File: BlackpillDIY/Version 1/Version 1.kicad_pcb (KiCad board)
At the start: 2 copper layers, 1 part, among them U1 STM32F411CCUx

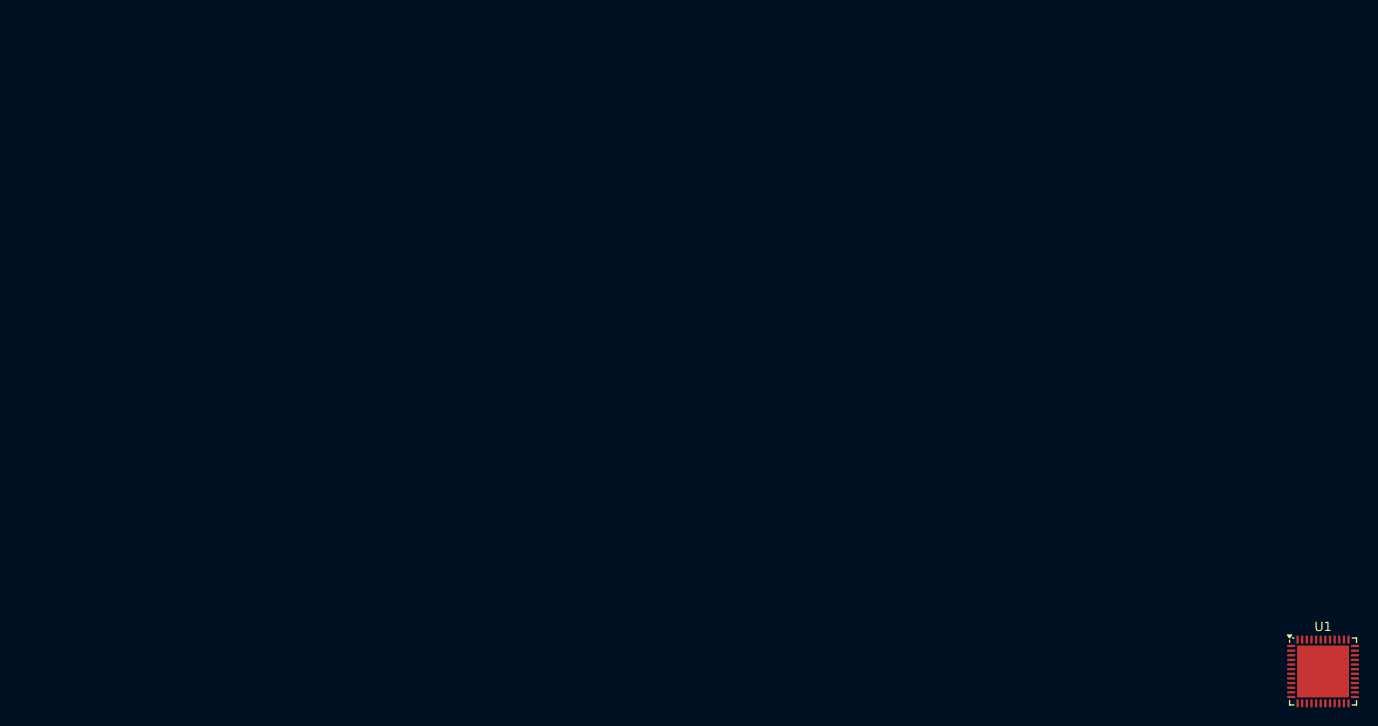
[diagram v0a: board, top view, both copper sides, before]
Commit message: Created THT PCB
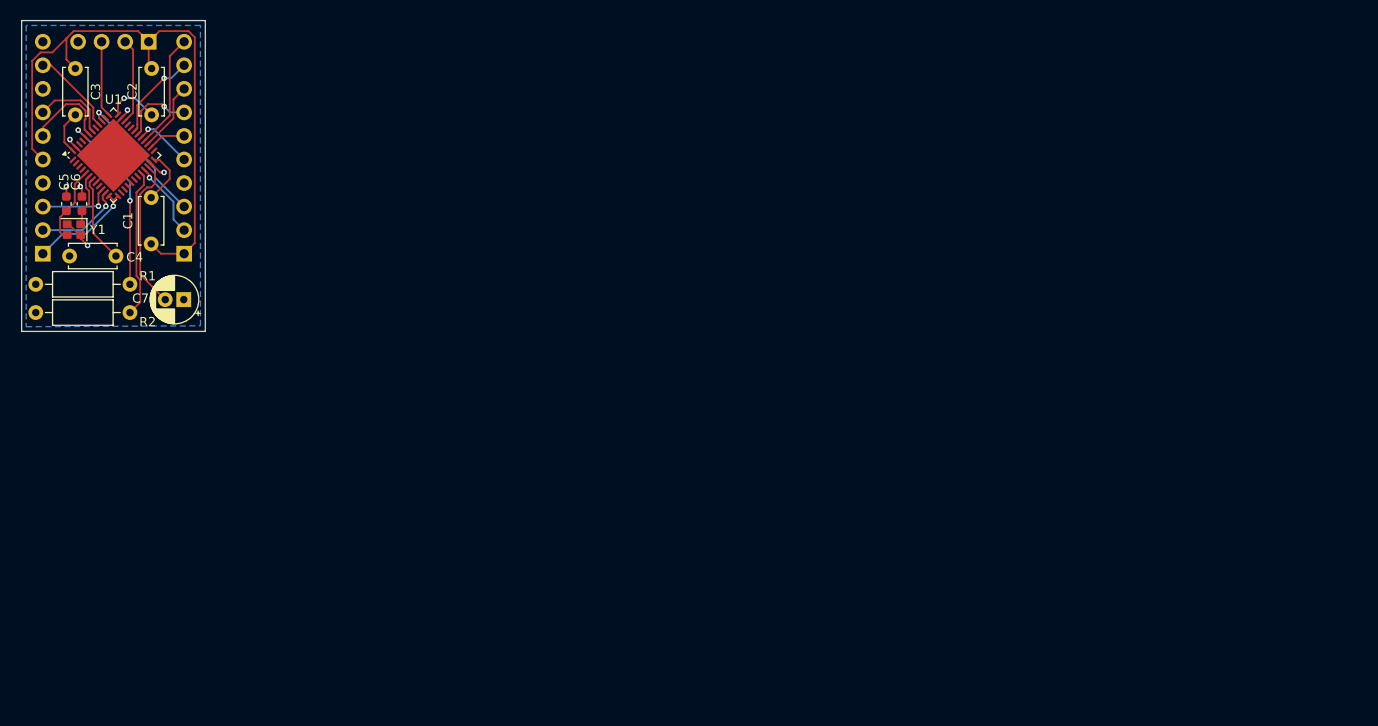
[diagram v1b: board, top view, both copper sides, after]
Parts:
- added C1: 100n, Capacitor_THT:C_Disc_D5.0mm_W2.5mm_P5.00mm, F.Cu at (27.6, 37.5)
- added C2: 100n, Capacitor_THT:C_Disc_D5.0mm_W2.5mm_P5.00mm, F.Cu at (27.7, 18.6)
- added C3: 100n, Capacitor_THT:C_Disc_D5.0mm_W2.5mm_P5.00mm, F.Cu at (19.5, 18.6)
- added C4: 100n, Capacitor_THT:C_Disc_D5.0mm_W2.5mm_P5.00mm, F.Cu at (18.8, 38.8)
- added C5: 12p, Capacitor_SMD:C_0603_1608Metric, F.Cu at (18.5, 33.2)
- added C6: 12p, Capacitor_SMD:C_0603_1608Metric, F.Cu at (20.2, 33.2)
- added C7: 2.2u, Capacitor_THT:CP_Radial_D5.0mm_P2.00mm, F.Cu at (31.2, 43.5)
- added J1: Left Header, Connector_PinHeader_2.54mm:PinHeader_1x10_P2.54mm_Vertical, B.Cu at (16.0, 38.5)
- added J2: Right Header, Connector_PinHeader_2.54mm:PinHeader_1x10_P2.54mm_Vertical, B.Cu at (31.2, 38.5)
- added J3: Debug, Connector_PinHeader_2.54mm:PinHeader_1x04_P2.54mm_Vertical, B.Cu at (27.4, 15.7)
- added R1: 10k, Resistor_THT:R_Axial_DIN0207_L6.3mm_D2.5mm_P10.16mm_Horizontal, F.Cu at (15.2, 41.8)
- added R2: 10k, Resistor_THT:R_Axial_DIN0207_L6.3mm_D2.5mm_P10.16mm_Horizontal, F.Cu at (15.2, 44.9)
- added Y1: Crystal_GND24, Crystal:Crystal_SMD_SeikoEpson_FA128-4Pin_2.0x1.6mm, F.Cu at (19.3, 36.0)
- moved U1 141.9 mm to (23.6, 27.9), turned to 45 degrees
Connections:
- U1 pad 10: unconnected-(U1-PA0-Pad10) -> TIM2_CH1
- U1 pad 11: unconnected-(U1-PA1-Pad11) -> TIM2_CH2
- U1 pad 12: unconnected-(U1-PA2-Pad12) -> TIM2_CH3
- U1 pad 13: unconnected-(U1-PA3-Pad13) -> TIM2_CH3
- U1 pad 20: unconnected-(U1-PB2-Pad20) -> /BOOT1
- U1 pad 21: unconnected-(U1-PB10-Pad21) -> I2C2_SCL
- U1 pad 22: unconnected-(U1-VCAP1-Pad22) -> /VCAP
- U1 pad 23: Net-(U1-VSS-Pad23) -> GND
- U1 pad 24: unconnected-(U1-VDD-Pad24) -> /VDD1
- U1 pad 26: unconnected-(U1-PB13-Pad26) -> TIM1_CH1N
- U1 pad 27: Net-(U1-PB14) -> TIM1_CH2N
- U1 pad 28: Net-(U1-PB15) -> TIM1_CH3N
- U1 pad 29: unconnected-(U1-PA8-Pad29) -> TIM1_CH1
- U1 pad 30: unconnected-(U1-PA9-Pad30) -> TIM1_CH2
- U1 pad 31: unconnected-(U1-PA10-Pad31) -> TIM1_CH3
- U1 pad 34: unconnected-(U1-PA13-Pad34) -> /SWDIO
- U1 pad 35: Net-(U1-VSS-Pad23) -> GND
- U1 pad 36: unconnected-(U1-VDD-Pad36) -> /VDD2
- U1 pad 37: unconnected-(U1-PA14-Pad37) -> /SWCLK
- U1 pad 39: unconnected-(U1-PB3-Pad39) -> I2C2_SDA
- U1 pad 40: unconnected-(U1-PB4-Pad40) -> EXTI4
- U1 pad 42: unconnected-(U1-PB6-Pad42) -> I2C1_SCL
- U1 pad 43: unconnected-(U1-PB7-Pad43) -> I2C1_SDA
- U1 pad 44: unconnected-(U1-BOOT0-Pad44) -> /BOOT0
- U1 pad 47: Net-(U1-VSS-Pad23) -> GND
- U1 pad 48: unconnected-(U1-VDD-Pad48) -> /VDD3
- U1 pad 49: Net-(U1-VSS-Pad23) -> GND
- U1 pad 5: Net-(U1-PH0) -> /RCC_IN
- U1 pad 6: Net-(U1-PH1) -> /RCC_OUT
- U1 pad 7: unconnected-(U1-NRST-Pad7) -> /RS
- U1 pad 8: unconnected-(U1-VSSA-Pad8) -> GND
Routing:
- net +3.3V: track 0.00 -> 65.7 mm
- net GND: track 0.00 -> 26.6 mm, vias 0 -> 6
- net /BOOT0: track 0.00 -> 20.1 mm, vias 0 -> 2
- net /VCAP: track 0.00 -> 16.8 mm
- net /BOOT1: track 0.00 -> 16.1 mm
- net I2C2_SDA: track 0.00 -> 15.1 mm, vias 0 -> 1
- net TIM1_CH3N: track 0.00 -> 12.5 mm
- net TIM2_CH3: track 0.00 -> 11.8 mm, vias 0 -> 1
- net TIM1_CH3: track 0.00 -> 9.77 mm, vias 0 -> 1
- net I2C1_SDA: track 0.00 -> 9.67 mm
- net TIM2_CH2: track 0.00 -> 9.64 mm, vias 0 -> 1
- net /RS: track 0.00 -> 9.57 mm
- net EXTI4: track 0.00 -> 9.43 mm
- net /SWDIO: track 0.00 -> 9.31 mm
- net /RCC_IN: track 0.00 -> 8.46 mm
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- added copper zone on B.Cu, net GND
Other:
- board outline added: 19.8 x 33.5 mm

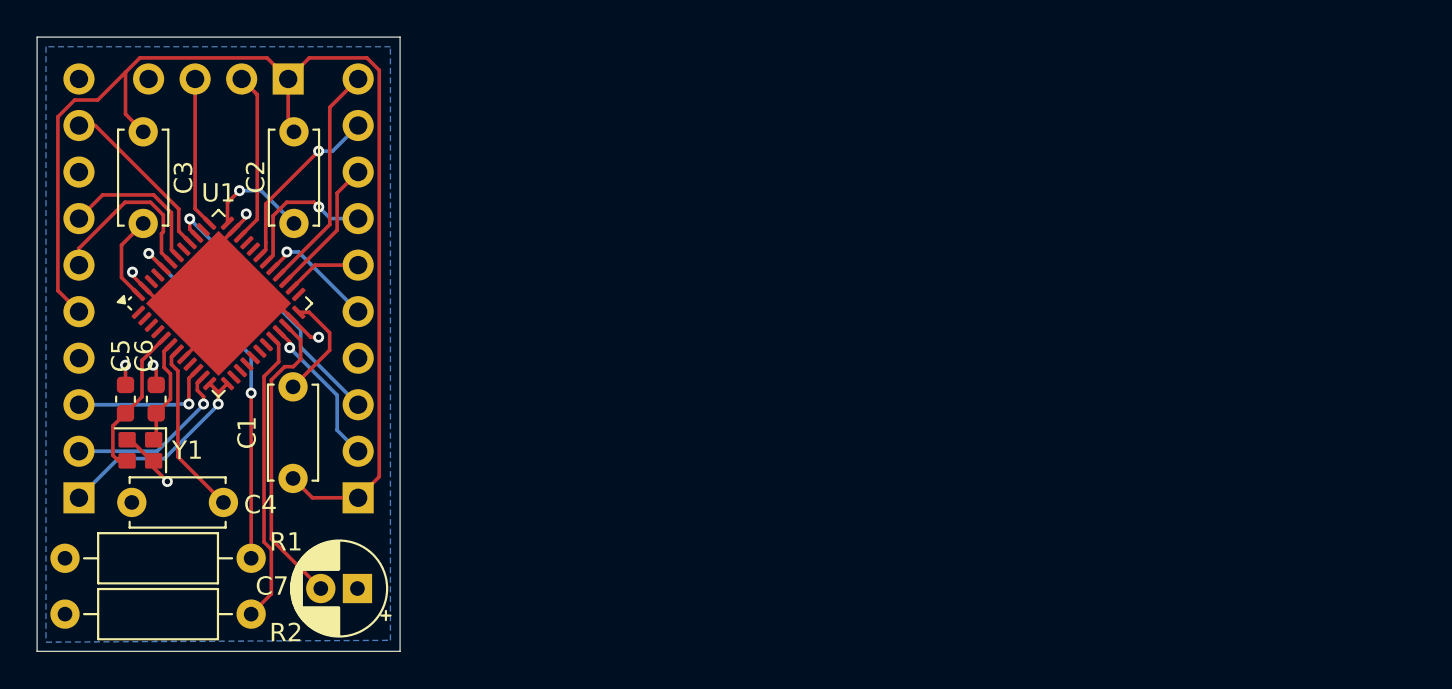
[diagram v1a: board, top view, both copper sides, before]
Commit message: Added breakouts for ESP Ublock and LIS.
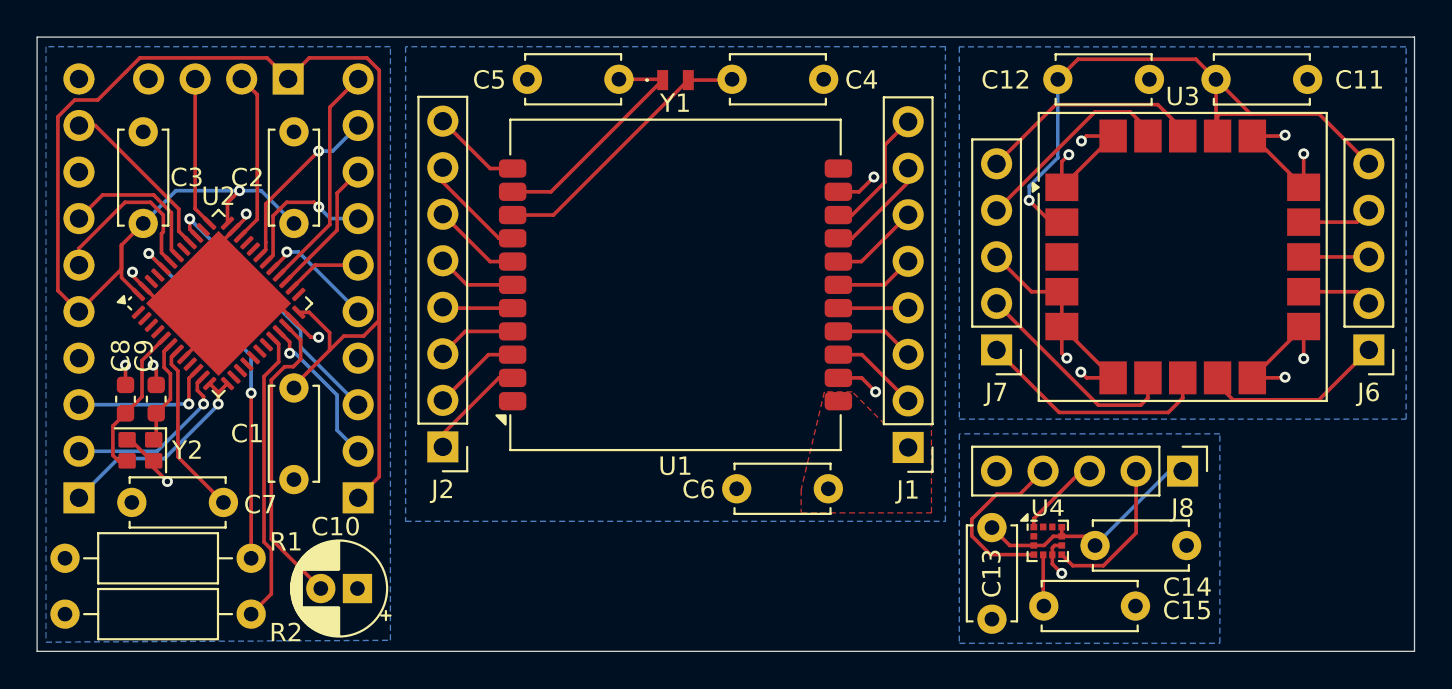
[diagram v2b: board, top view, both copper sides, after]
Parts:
- added C11: 100n, Capacitor_THT:C_Disc_D5.0mm_W2.5mm_P5.00mm, F.Cu at (78.0, 15.7)
- added C12: 100n, Capacitor_THT:C_Disc_D5.0mm_W2.5mm_P5.00mm, F.Cu at (69.4, 15.7)
- added C13: 100n, Capacitor_THT:C_Disc_D5.0mm_W2.5mm_P5.00mm, F.Cu at (65.8, 40.2)
- added C14: 100n, Capacitor_THT:C_Disc_D5.0mm_W2.5mm_P5.00mm, F.Cu at (71.4, 41.2)
- added C15: 100n, Capacitor_THT:C_Disc_D5.0mm_W2.5mm_P5.00mm, F.Cu at (68.6, 44.5)
- added C4: 22p, Capacitor_THT:C_Disc_D5.0mm_W2.5mm_P5.00mm, F.Cu at (51.6, 15.7)
- added C5: 22p, Capacitor_THT:C_Disc_D5.0mm_W2.5mm_P5.00mm, F.Cu at (45.4, 15.7)
- added C6: 100n, Capacitor_THT:C_Disc_D5.0mm_W2.5mm_P5.00mm, F.Cu at (56.9, 38.1)
- added J1: Conn_01x08, Connector_PinHeader_2.54mm:PinHeader_1x08_P2.54mm_Vertical, F.Cu at (61.2, 35.8)
- added J2: Conn_01x08, Connector_PinHeader_2.54mm:PinHeader_1x08_P2.54mm_Vertical, F.Cu at (35.8, 35.8)
- added J6: Conn_01x05, Connector_PinHeader_2.54mm:PinHeader_1x05_P2.54mm_Vertical, F.Cu at (86.4, 30.5)
- added J7: Conn_01x05, Connector_PinHeader_2.54mm:PinHeader_1x05_P2.54mm_Vertical, F.Cu at (66.0, 30.5)
- added J8: Conn_01x05, Connector_PinHeader_2.54mm:PinHeader_1x05_P2.54mm_Vertical, F.Cu at (76.2, 37.1)
- added U1: HT-CT62, RF_Module:Heltec_HT-CT62, F.Cu at (48.5, 26.9)
- added U3: SAM-M8Q, RF_GPS:ublox_SAM-M8Q, F.Cu at (76.2, 25.4)
- added U4: LIS2MDL, Package_LGA:LGA-12_2x2mm_P0.5mm, F.Cu at (68.8, 40.9)
- added Y1: LFXTAL062558Reel, LIB_LFXTAL062558Reel:LFXTAL062558Reel, F.Cu at (48.5, 15.7)
- moved C2 5.00 mm to (27.7, 23.6), turned to 90 degrees
- moved C3 5.00 mm to (19.5, 23.6), turned to 90 degrees
- moved C1 4.94 mm to (27.7, 32.6), turned to -90 degrees
- renumbered C7 to C10, C4 to C7, C5 to C8, C6 to C9, J1 to J4, J2 to J5, U1 to U2, Y1 to Y2
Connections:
- C1 pad 1: +3.3V -> +3.3V1
- C1 pad 2: /VDD1 -> GND1
- C10 pad 1: GND -> GND1
- C2 pad 1: +3.3V -> +3.3V1
- C2 pad 2: /VDD2 -> GND1
- C3 pad 1: +3.3V -> +3.3V1
- C3 pad 2: /VDD3 -> GND1
- C7 pad 1: GND -> GND1
- C8 pad 1: GND -> GND1
- C9 pad 1: GND -> GND1
- J3 pad 1: +3.3V -> +3.3V1
- J4 pad 4: GND -> GND1
- J4 pad 5: +3.3V -> +3.3V1
- J4 pad 8: GND -> GND1
- J5 pad 1: +3.3V -> +3.3V1
- J5 pad 4: GND -> GND1
- R1 pad 1: GND -> GND1
- R2 pad 1: GND -> GND1
- U2 pad 23: GND -> GND1
- U2 pad 24: /VDD1 -> +3.3V1
- U2 pad 35: GND -> GND1
- U2 pad 36: /VDD2 -> +3.3V1
- U2 pad 47: GND -> GND1
- U2 pad 48: /VDD3 -> +3.3V1
- U2 pad 49: GND -> GND1
- U2 pad 8: GND -> GND1
- Y2 pad 2: GND -> GND1
- Y2 pad 4: GND -> GND1
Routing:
- net +3.3V1: track 0.00 -> 86.4 mm, vias 0 -> 1
- net +3.3V: track 65.7 -> 0.00 mm
- net GND3: track 0.00 -> 37.1 mm, vias 0 -> 8
- net +3.3V3: track 0.00 -> 35.4 mm, vias 0 -> 1
- net GND1: track 0.00 -> 27.0 mm, vias 0 -> 6
- net GND: track 26.6 -> 0.00 mm, vias 6 -> 0
- net /GPIO1: track 0.00 -> 15.0 mm
- net +3.3V4: track 0.00 -> 13.4 mm
- net /GPIO0: track 0.00 -> 13.1 mm
- net /SBOOT: track 0.00 -> 13.0 mm
- net /RST: track 0.00 -> 12.4 mm
- net /TPULSE: track 0.00 -> 11.8 mm
- net /EXTINT: track 0.00 -> 11.2 mm
- net GND2: track 0.00 -> 10.4 mm, vias 0 -> 2
- net /SDA1: track 0.00 -> 10.1 mm
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- added copper zone on F.Cu, net +3.3V2
- added copper zone on B.Cu, net GND1
- added copper zone on B.Cu, net GND2
- added copper zone on B.Cu, net GND3
- added copper zone on B.Cu, net GND4
- removed copper zone on B.Cu, net GND
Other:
- board size 19.8 x 33.5 mm -> 75.2 x 33.5 mm

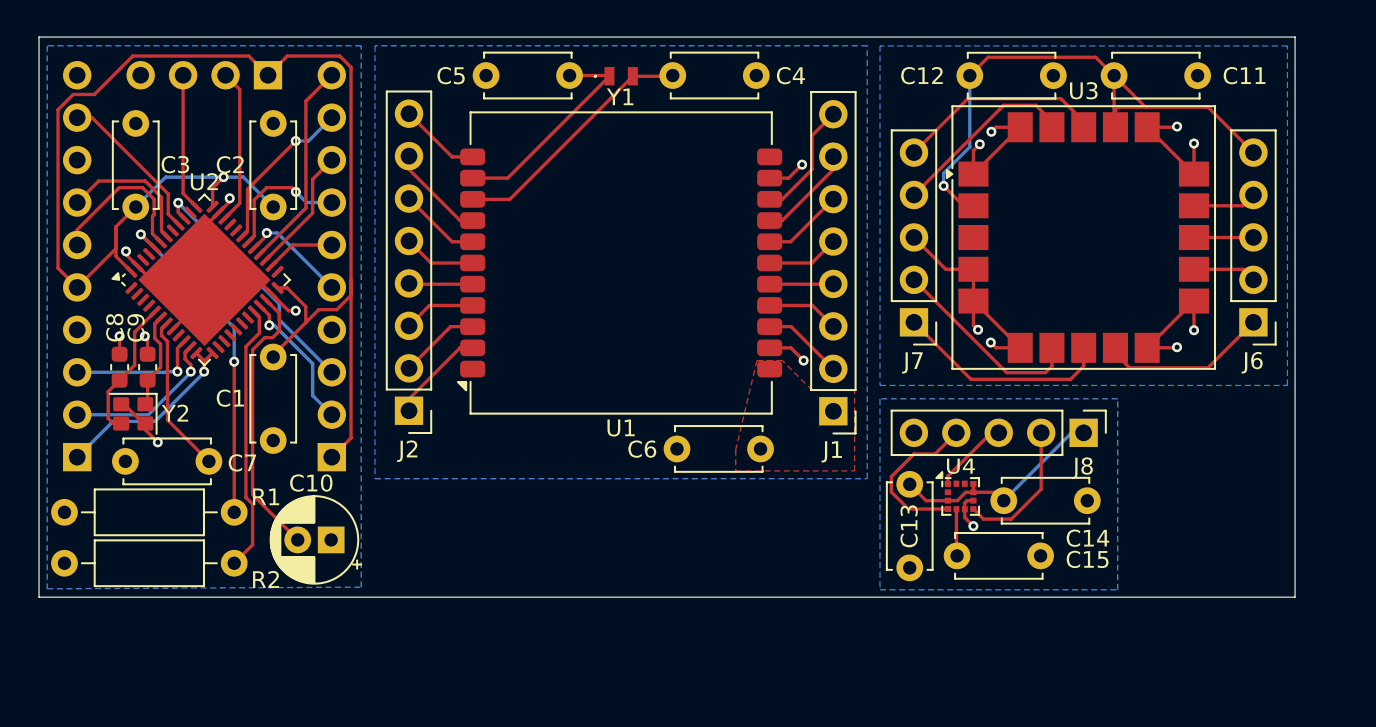
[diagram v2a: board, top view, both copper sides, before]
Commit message: Added silkscreen and autoboot for esp
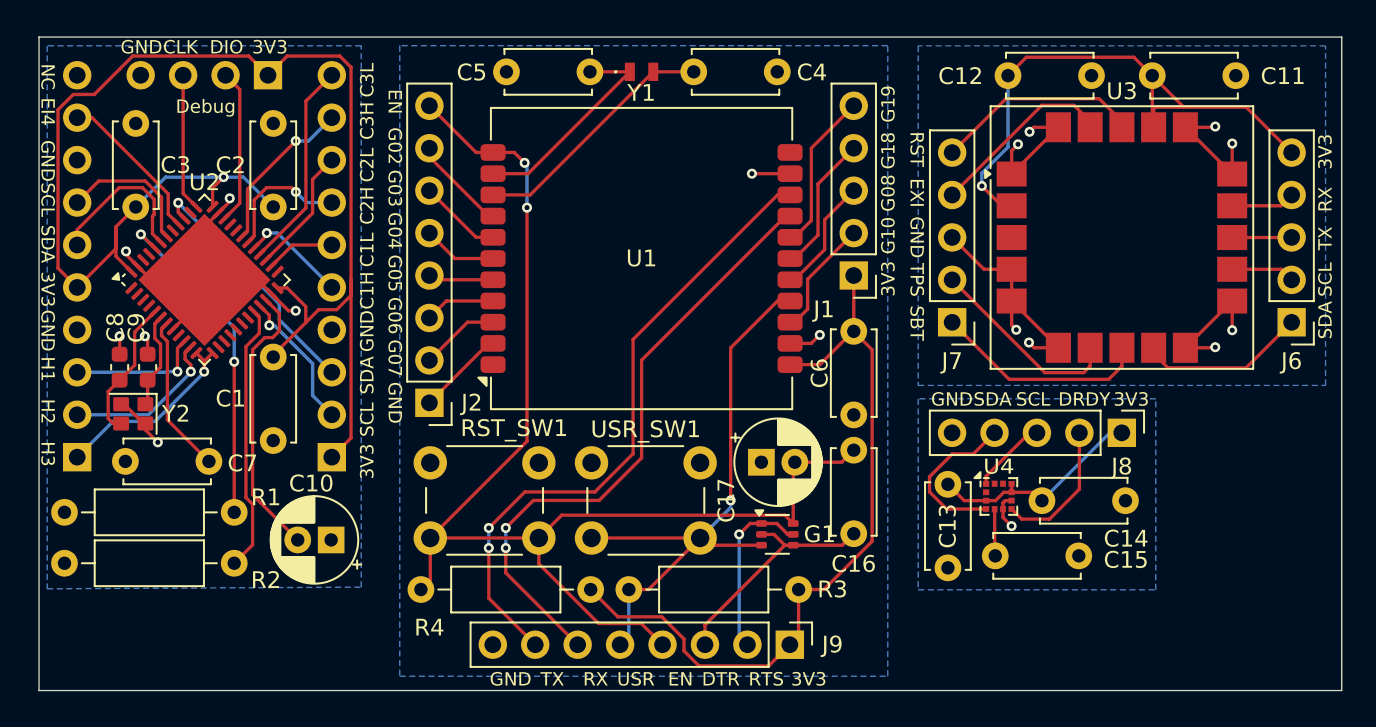
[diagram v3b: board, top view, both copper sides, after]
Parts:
- added C16: 100n, Capacitor_THT:C_Disc_D5.0mm_W2.5mm_P5.00mm, F.Cu at (62.4, 43.1)
- added C17: 2.2u, Capacitor_THT:CP_Radial_D5.0mm_P2.00mm, F.Cu at (56.9, 38.9)
- added G1: 2N7002BKS, Package_TO_SOT_SMD:SOT-363_SC-70-6, F.Cu at (57.9, 43.2)
- added J9: Conn_01x08, Connector_PinHeader_2.54mm:PinHeader_1x08_P2.54mm_Vertical, F.Cu at (58.6, 49.8)
- added R3: 10k, Resistor_THT:R_Axial_DIN0207_L6.3mm_D2.5mm_P10.16mm_Horizontal, F.Cu at (49.0, 46.5)
- added R4: 10k, Resistor_THT:R_Axial_DIN0207_L6.3mm_D2.5mm_P10.16mm_Horizontal, F.Cu at (46.7, 46.5)
- added RST_SW1: RESET_SW, Button_Switch_THT:SW_PUSH_6mm_H4.3mm, F.Cu at (37.1, 38.9)
- added USR_SW1: RESET_SW, Button_Switch_THT:SW_PUSH_6mm_H4.3mm, F.Cu at (46.7, 38.9)
- J1: footprint Connector_PinHeader_2.54mm:PinHeader_1x08_P2.54mm_Vertical -> Connector_PinHeader_2.54mm:PinHeader_1x05_P2.54mm_Vertical
- moved C6 8.98 mm to (62.4, 31.0), turned to -90 degrees
- moved J1 8.22 mm to (62.4, 27.7)
- moved C11 2.29 mm to (80.3, 15.7)
- moved C12 2.29 mm to (71.7, 15.7)
- moved C13 2.29 mm to (68.1, 40.2)
- moved C14 2.29 mm to (73.7, 41.2)
- moved C15 2.29 mm to (70.9, 44.5)
- moved J6 2.29 mm to (88.6, 30.5)
- moved J8 2.29 mm to (78.5, 37.1)
- moved U3 2.29 mm to (78.5, 25.4)
- moved U4 2.29 mm to (71.1, 40.9)
- moved J7 2.29 mm to (68.3, 30.5)
- moved J2 1.31 mm to (37.0, 35.3)
- moved C4 1.27 mm to (52.9, 15.5)
- moved Y1 1.25 mm to (49.7, 15.5)
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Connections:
- J1 pad 3: /GPIO9 -> /GPIO8
- J1 pad 4: /GPIO8 -> /GPIO18
- J1 pad 5: /GPIO18 -> /GPIO19
- U1 pad 15: /GPIO9 -> /USR_Key
- U1 pad 19: /GPIO20 -> /RX
- U1 pad 20: /GPIO21 -> /TX
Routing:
- net /ESPEN: track 4.88 -> 76.3 mm, vias 0 -> 2
- net +3.3V2: track 0.00 -> 44.9 mm
- net /TX: track 0.00 -> 38.4 mm, vias 0 -> 2
- net /RX: track 0.00 -> 36.9 mm, vias 0 -> 2
- net /USR_Key: track 0.00 -> 36.3 mm, vias 0 -> 1
- net /DTR: track 0.00 -> 14.0 mm
- net /RTS: track 0.00 -> 10.6 mm, vias 0 -> 1
- net /GPIO21: track 7.11 -> 0.00 mm
- net /GPIO20: track 5.84 -> 0.00 mm
- net /GPIO19: track 4.87 -> 9.61 mm
- net /GPIO9: track 4.33 -> 0.00 mm
- net /GPIO18: track 4.34 -> 8.34 mm
- net /GPIO8: track 3.82 -> 7.07 mm
- net /GPIO10: track 4.86 -> 7.07 mm
- net GND2: track 10.4 -> 9.56 mm
- removed copper zone on F.Cu, net +3.3V2
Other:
- board size 75.2 x 33.5 mm -> 78 x 39.1 mm
- board text added: "3V3"
- board text added: "C1H"
- board text added: "C1L"
- board text added: "C2H"
- board text added: "C2L"
- board text added: "C3H"
- board text added: "C3L"
- board text added: "CLK"
- board text added: "DIO"
- board text added: "DRDY"
- board text added: "DTR"
- board text added: "Debug"
- board text added: "EI4"
- board text added: "EN"
- board text added: "EXI"
- board text added: "G02"
- board text added: "G03"
- board text added: "G04"
- board text added: "G05"
- board text added: "G06"
- board text added: "G07"
- board text added: "G08"
- board text added: "G10"
- board text added: "G18"
- board text added: "G19"
- board text added: "GND"
- board text added: "H1"
- board text added: "H2"
- board text added: "H3"
- board text added: "NC"
- board text added: "RST"
- board text added: "RTS"
- board text added: "RX"
- board text added: "SBT"
- board text added: "SCL"
- board text added: "SDA"
- board text added: "TPS"
- board text added: "TX"
- board text added: "USR"
